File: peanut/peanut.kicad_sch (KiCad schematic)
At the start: 34 parts, among them J1 USB-C, Q1 NMOS, U1 ESP32-C3FH4, U3 MS5611-01BA, Y1 32.768kHz, Y2 40MHz

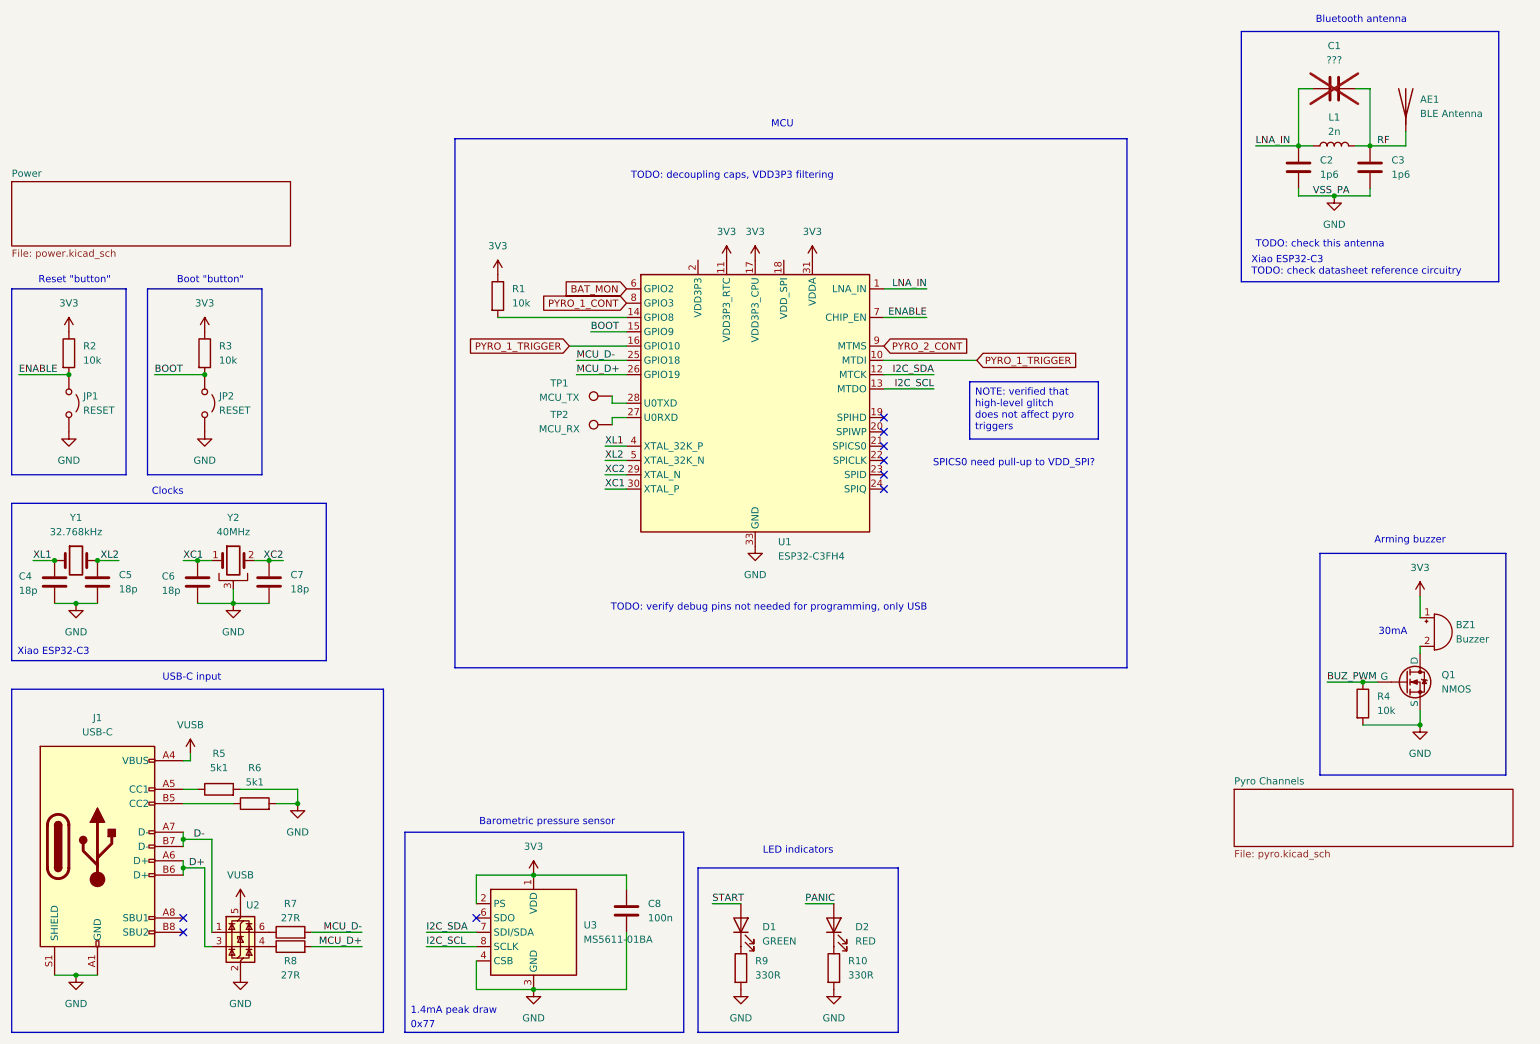
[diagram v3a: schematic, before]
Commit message: feat: Finish schematic
This commit "completes" the schematic to the best of my foresight for
the moment. All components have BOM MPNs and footprints assigned. I have
double checked pins on the 40MHz clock and that pin assignments on the
MCU are valid. I have selected a chip antenna with high gain, added
decoupling capacitors to the MCU, picked out terminal blocks and
followed the Espressif schematic guide. A preliminary layout can be
made.
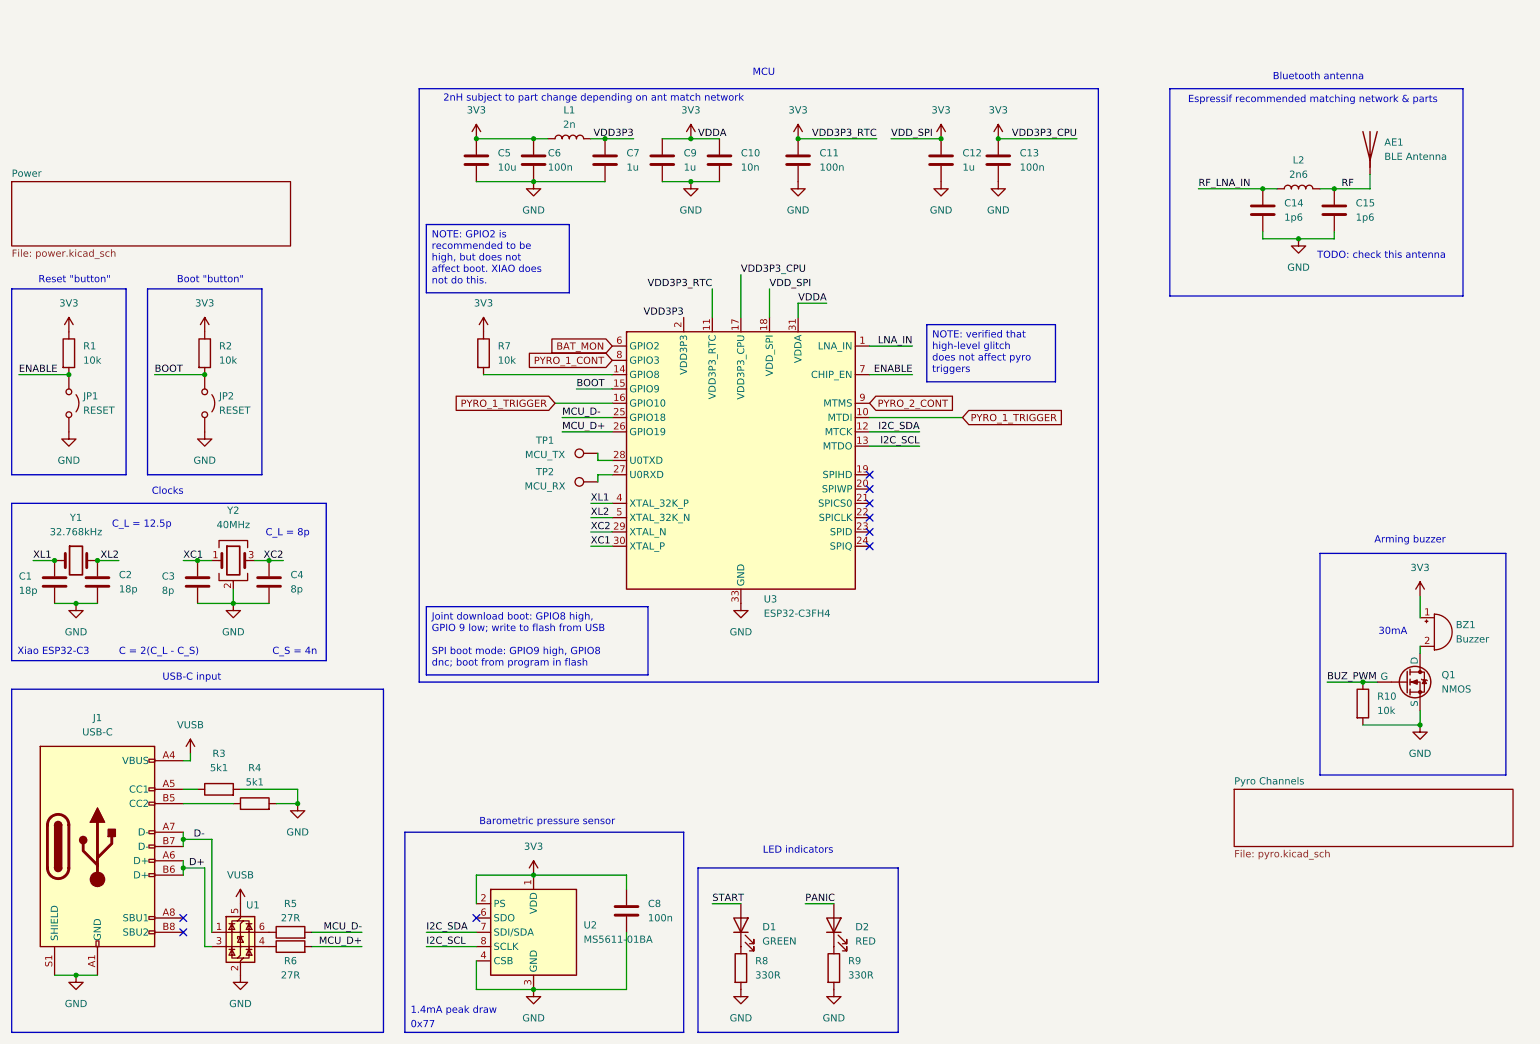
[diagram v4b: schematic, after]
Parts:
- removed C1: ???, Capacitor_SMD:C_0402_1005Metric, symbol Device:C
- removed C2: 1p6, Capacitor_SMD:C_0402_1005Metric, symbol Device:C
- added C10: 10n, Capacitor_SMD:C_0402_1005Metric, symbol Device:C
- added C11, C13, C6: 100n, Capacitor_SMD:C_0402_1005Metric, symbol Device:C
- added C12, C7, C9: 1u, Capacitor_SMD:C_0603_1608Metric, symbol Device:C
- added C14: 1p6, Capacitor_SMD:C_0201_0603Metric_Pad0.64x0.40mm_HandSolder, symbol Device:C
- added C5: 10u, Capacitor_SMD:C_0603_1608Metric, symbol Device:C
- added L1: 2n, Inductor_SMD:L_01005_0402Metric, symbol Device:L
- AE1: footprint Resistor_SMD:R_1206_3216Metric -> ACAG0201-2450-T:ANTC2012X70N; MPN (none) -> ACAG0201-2450-T
- BZ1: footprint (none) -> CMI-0955-03TH:CMI095503TH
- C1: renamed from C4; MPN (none) -> GJM0225C1C180JB01L
- C15: renamed from C3; footprint Capacitor_SMD:C_0402_1005Metric -> Capacitor_SMD:C_0201_0603Metric_Pad0.64x0.40mm_HandSolder; MPN (none) -> GRM0335C1H1R6BA01D
- C2: renamed from C5; MPN (none) -> GJM0225C1C180JB01L
- C3: renamed from C6; value 18p -> 8p; MPN (none) -> GRM1555C1E8R0DA01D
- C4: renamed from C7; value 18p -> 8p; MPN (none) -> GRM1555C1E8R0DA01D
- JP1, JP2, TP1, TP2: MPN (none) -> -
- L2: renamed from L1; value 2n -> 2n6; footprint (none) -> Inductor_SMD:L_0201_0603Metric_Pad0.64x0.40mm_HandSolder; MPN (none) -> LQP03TN2N6B02D
- Q1: MPN BSS138IXTSA1 -> BSS123NH6327XTSA1
- U1: renamed from U2; value ~ -> (none)
- Y2: footprint (none) -> Crystal:Crystal_SMD_2016-4Pin_2.0x1.6mm; symbol Device:Crystal_GND3 -> Device:Crystal_GND24; MPN (none) -> 830108213209
- renumbered R2 to R1, R4 to R10, R3 to R2, R5 to R3, R6 to R4, R7 to R5, R8 to R6, R1 to R7, R9 to R8, R10 to R9, U3 to U2, U1 to U3
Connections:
- net 3V3: now also U3.18 (VDD_SPI), C10.1, C11.1, C12.1, C13.1, C5.1, C6.1, C9.1, L1.1
- net GND: now also Y2.2 (G), Y2.4 (G), C10.2, C11.2, C12.2, C13.2, C14.2, C5.2, C6.2, C7.2, C9.2; no longer Y2.3
- net LNA_IN: no longer L2.1
- net XC2: now also Y2.3; no longer Y2.2
- net VDD3P3: now reaches U3.2 (VDD3P3), U3.3 (VDD3P3)
- net VDD3P3: now also C7.1, L1.2
- new net RF_LNA_IN: C14.1, L2.1
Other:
- note added: "2nH subject to part change depending on ant match network"
- note added: "C = 2(C_L - C_S)"
- note added: "C_L = 12.5p"
- note added: "C_L = 8p"
- note added: "C_S = 4n"
- note added: "Espressif recommended matching network & parts"
- note removed: "SPICS0 need pull-up to VDD_SPI?"
- note removed: "TODO: decoupling caps, VDD3P3 filtering"
- note removed: "TODO: verify debug pins not needed for programming, only USB"
- note removed: "Xiao ESP32-C3 TODO: check datasheet reference circuitry"
- moved on the sheet: AE1, C15, L2, R7, TP1, TP2, U3

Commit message: feat: Initial layout
I have roughed out the initial PCB layout. It is wider than I'd like,
and not near a peanut shape. It appears the "start" and "panic" LEDs
never had pins assigned to them. I think I will replace the MCU RX & TX
with these instead, since I can still use the RX and TX as probe pads
that way.
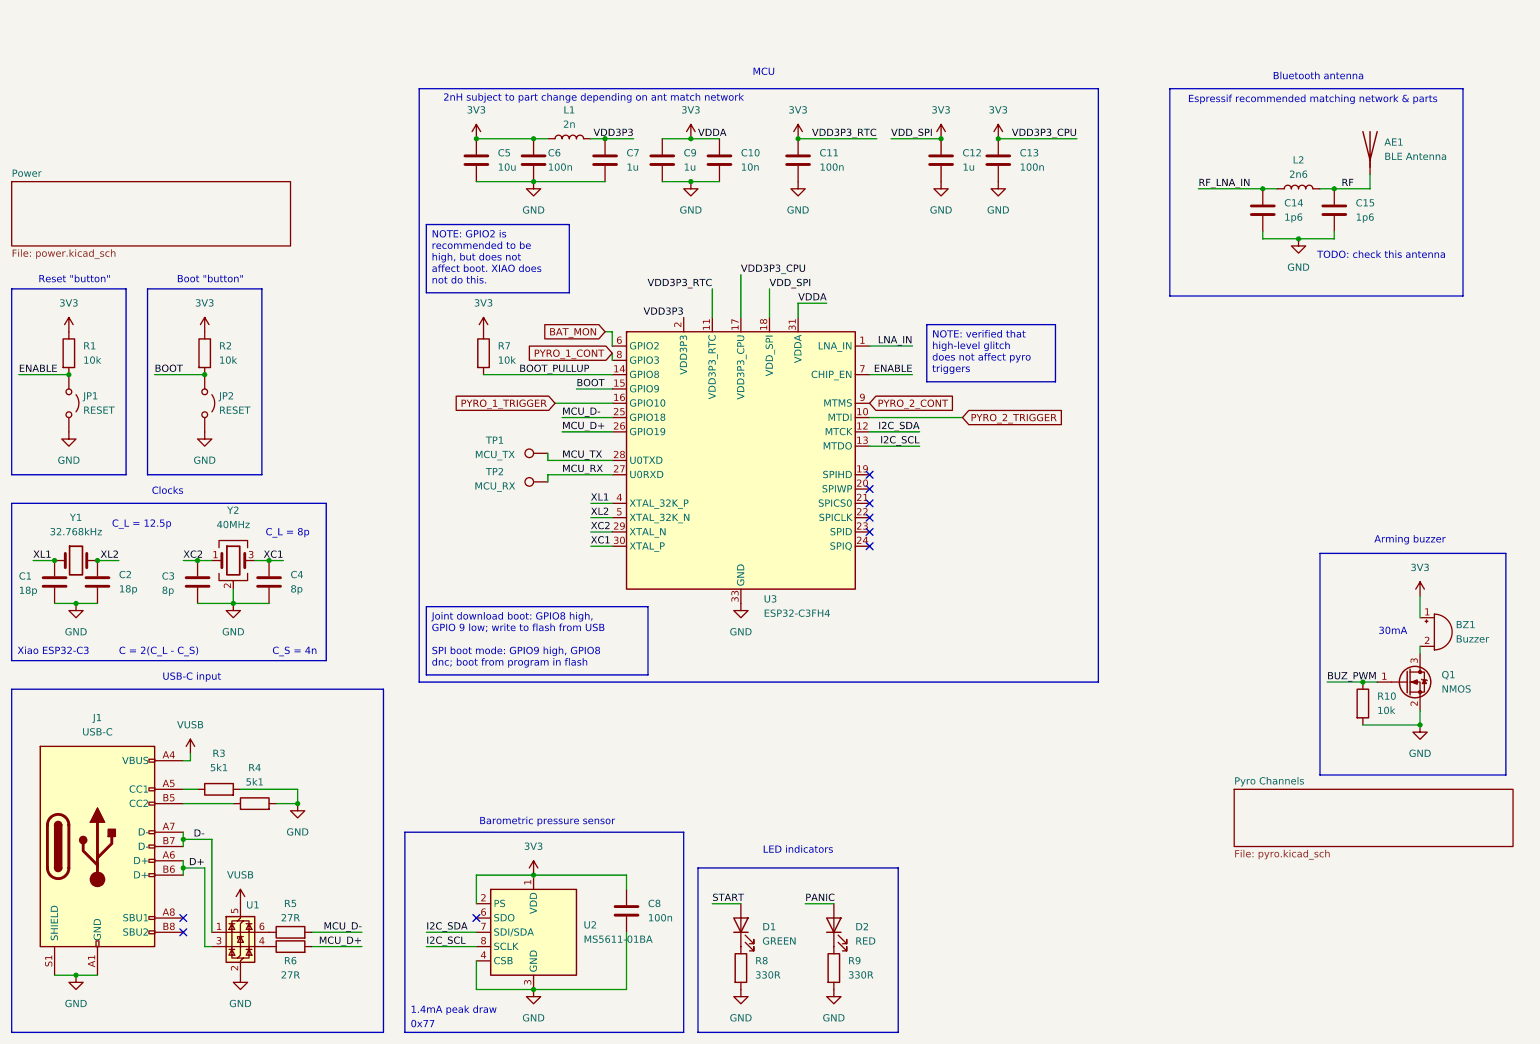
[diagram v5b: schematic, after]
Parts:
- Q1: symbol Simulation_SPICE:NMOS -> Transistor_FET_Other:Q_NMOS_Depletion_GSD
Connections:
- net BUZ_PWM: now also Q1.1 (G); no longer Q1.2 (G)
- net GND: now also Q1.2 (S); no longer Q1.3 (S)
- net PYRO_1_TRIGGER: no longer U3.10 (MTDI)
- net XC1: now also C4.1, Y2.3; no longer C3.1, Y2.1
- net XC2: now also C3.1, Y2.1; no longer C4.1, Y2.3
- net at BZ1.2 (-): now also Q1.3 (D); no longer Q1.1 (D)
- net MCU_RX: now reaches TP2.1, U3.27 (U0RXD)
- net MCU_TX: now reaches TP1.1, U3.28 (U0TXD)
- net BOOT_PULLUP: now reaches R7.2, U3.14 (GPIO8)
- new net PYRO_2_TRIGGER: U3.10 (MTDI)
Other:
- moved on the sheet: TP1, TP2
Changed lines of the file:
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@@
 	(wire
 		(pts
-			(xy 119.38 96.52) (xy 119.38 97.79)
+			(xy 110.49 96.52) (xy 110.49 97.79)
 		)
 		(stroke
@@
 	(wire
 		(pts
+			(xy 120.65 71.12) (xy 121.92 71.12)
+		)
+		(stroke
+			(width 0)
+			(type default)
+		)
+	)
+	(wire
+		(pts
 			(xy 130.81 36.83) (xy 135.89 36.83)
 		)
@@
 	(wire
 		(pts
-			(xy 119.38 92.71) (xy 119.38 93.98)
+			(xy 110.49 92.71) (xy 110.49 93.98)
 		)
 		(stroke
@@
 	(wire
 		(pts
+			(xy 121.92 74.93) (xy 121.92 76.2)
+		)
+		(stroke
+			(width 0)
+			(type default)
+		)
+	)
+	(wire
+		(pts
 			(xy 49.53 180.34) (xy 49.53 166.37)
 		)
@@
 	(wire
 		(pts
-			(xy 119.38 93.98) (xy 121.92 93.98)
+			(xy 110.49 93.98) (xy 121.92 93.98)
 		)
 		(stroke
@@
 	(wire
 		(pts
+			(xy 121.92 71.12) (xy 121.92 73.66)
+		)
+		(stroke
+			(width 0)
+			(type default)
+		)
+	)
+	(wire
+		(pts
 			(xy 154.94 66.04) (xy 154.94 68.58)
 		)
@@
 	(wire
 		(pts
-			(xy 121.92 96.52) (xy 119.38 96.52)
+			(xy 121.92 96.52) (xy 110.49 96.52)
 		)
 		(stroke
@@
 		)
 	)
+	(label "BOOT_PULLUP"
+		(at 105.41 78.74 0)
+		(effects
+			(font
+				(size 1.27 1.27)
+			)
+			(justify left bottom)
+		)
+	)
 	(label "I2C_SCL"
 		(at 176.53 91.44 180)
@@
 		)
 	)
+	(label "XC2"
+		(at 45.72 111.76 0)
+		(effects
+			(font
+				(size 1.27 1.27)
+			)
+			(justify left bottom)
+		)
+	)
 	(label "MCU_D+"
 		(at 77.47 180.34 180)
@@
 		)
 	)
-	(label "XC1"
-		(at 45.72 111.76 0)
+	(label "MCU_TX"
+		(at 113.03 93.98 0)
+		(effects
+			(font
+				(size 1.27 1.27)
+			)
+			(justify left bottom)
+		)
+	)
+	(label "MCU_RX"
+		(at 113.03 96.52 0)
 		(effects
 			(font
@@
 		)
 	)
+	(label "XC1"
+		(at 63.5 111.76 180)
+		(effects
+			(font
+				(size 1.27 1.27)
+			)
+			(justify right bottom)
+		)
+	)
 	(label "RF"
 		(at 251.46 45.72 0)
@@
 		)
 	)
-	(label "XC2"
-		(at 63.5 111.76 180)
-		(effects
-			(font
-				(size 1.27 1.27)
-			)
-			(justify right bottom)
-		)
-	)
 	(label "I2C_SCL"
 		(at 88.9 180.34 0)
@@
 	(global_label "BAT_MON"
 		(shape input)
-		(at 121.92 73.66 180)
+		(at 120.65 71.12 180)
 		(fields_autoplaced yes)
 		(effects
@@
 		)
 		(property "Intersheetrefs" "${INTERSHEET_REFS}"
-			(at 110.5286 73.66 0)
+			(at 109.2586 71.12 0)
 			(hide yes)
 			(show_name no)
@@
 		)
 	)
-	(global_label "PYRO_1_TRIGGER"
+	(global_label "PYRO_2_TRIGGER"
 		(shape input)
 		(at 184.15 86.36 0)
@@
 	(global_label "PYRO_1_CONT"
 		(shape input)
-		(at 121.92 76.2 180)
+		(at 121.92 74.93 180)
 		(fields_autoplaced yes)
 		(effects
@@
 		)
 		(property "Intersheetrefs" "${INTERSHEET_REFS}"
-			(at 105.9324 76.2 0)
+			(at 105.9324 74.93 0)
 			(hide yes)
 			(show_name no)
@@
 	)
 	(symbol
-		(lib_id "Simulation_SPICE:NMOS")
+		(lib_id "Transistor_FET_Other:Q_NMOS_Depletion_GSD")
 		(at 262.89 133.35 0)
 		(unit 1)
@@
 		)
 		(property "Footprint" "Package_TO_SOT_SMD:SOT-23-3"
-			(at 267.97 130.81 0)
+			(at 262.89 133.35 0)
 			(hide yes)
 			(show_name no)
@@
 		)
 		(property "Datasheet" "https://www.mouser.ca/datasheet/3/70/1/Infineon_BSS123N_DataSheet_v02_03_en.pdf"
-			(at 262.89 146.05 0)
-			(hide yes)
-			(show_name no)
-			(do_not_autoplace no)
-			(effects
-				(font
-					(size 1.27 1.27)
-				)
-			)
-		)
-		(property "Description" "N-MOSFET transistor, drain/source/gate"
+			(at 262.89 133.35 0)
+			(hide yes)
+			(show_name no)
+			(do_not_autoplace no)
+			(effects
+				(font
+					(size 1.27 1.27)
+				)
+			)
+		)
+		(property "Description" "Depletion-mode N-channel MOSFET gate/source/drain"
 			(at 262.89 133.35 0)
 			(hide yes)
@@
 	(symbol
 		(lib_id "Connector:TestPoint")
-		(at 119.38 97.79 90)
+		(at 110.49 97.79 90)
 		(unit 1)
 		(body_style 1)
@@
 		(dnp no)
 		(property "Reference" "TP2"
-			(at 109.982 96.012 90)
+			(at 101.092 96.012 90)
 			(show_name no)
 			(do_not_autoplace no)
@@
 		)
 		(property "Value" "MCU_RX"
-			(at 109.982 98.552 90)
+			(at 101.092 98.552 90)
 			(show_name no)
 			(do_not_autoplace no)
@@
 		)
 		(property "Footprint" "TestPoint:TestPoint_Pad_D1.0mm"
-			(at 119.38 92.71 0)
+			(at 110.49 92.71 0)
 			(hide yes)
 			(show_name no)
@@
 		)
 		(property "Datasheet" ""
-			(at 119.38 92.71 0)
+			(at 110.49 92.71 0)
 			(hide yes)
 			(show_name no)
@@
 		)
 		(property "Description" "test point"
-			(at 119.38 97.79 0)
+			(at 110.49 97.79 0)
 			(hide yes)
 			(show_name no)
@@
 		)
 		(property "MPN" "-"
-			(at 119.38 97.79 90)
+			(at 110.49 97.79 90)
 			(hide yes)
 			(show_name no)
@@
 	(symbol
 		(lib_id "Connector:TestPoint")
-		(at 119.38 92.71 90)
+		(at 110.49 92.71 90)
 		(unit 1)
 		(body_style 1)
@@
 		(dnp no)
 		(property "Reference" "TP1"
-			(at 109.982 90.424 90)
+			(at 101.092 90.424 90)
 			(show_name no)
 			(do_not_autoplace no)
@@
 		)
 		(property "Value" "MCU_TX"
-			(at 109.982 92.964 90)
+			(at 101.092 92.964 90)
 			(show_name no)
 			(do_not_autoplace no)
@@
 		)
 		(property "Footprint" "TestPoint:TestPoint_Pad_D1.0mm"
-			(at 119.38 87.63 0)
+			(at 110.49 87.63 0)
 			(hide yes)
 			(show_name no)
@@
 		)
 		(property "Datasheet" ""
-			(at 119.38 87.63 0)
+			(at 110.49 87.63 0)
 			(hide yes)
 			(show_name no)
@@
 		)
 		(property "Description" "test point"
-			(at 119.38 92.71 0)
+			(at 110.49 92.71 0)
 			(hide yes)
 			(show_name no)
@@
 		)
 		(property "MPN" "-"
-			(at 119.38 92.71 90)
-			(hide yes)
-			(show_name no)
+			(at 110.49 92.71 90)
+			(hide yes)
+			(show_name no)
